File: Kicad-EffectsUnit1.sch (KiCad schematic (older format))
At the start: 114 parts, among them J101 In7, J102 Doepfer connector, J103 Vin 7-12v, J104 In6, J105 In3, J106 Out10, J107 Out11, J108 Out9, J109 Out6, J110 Power Conn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

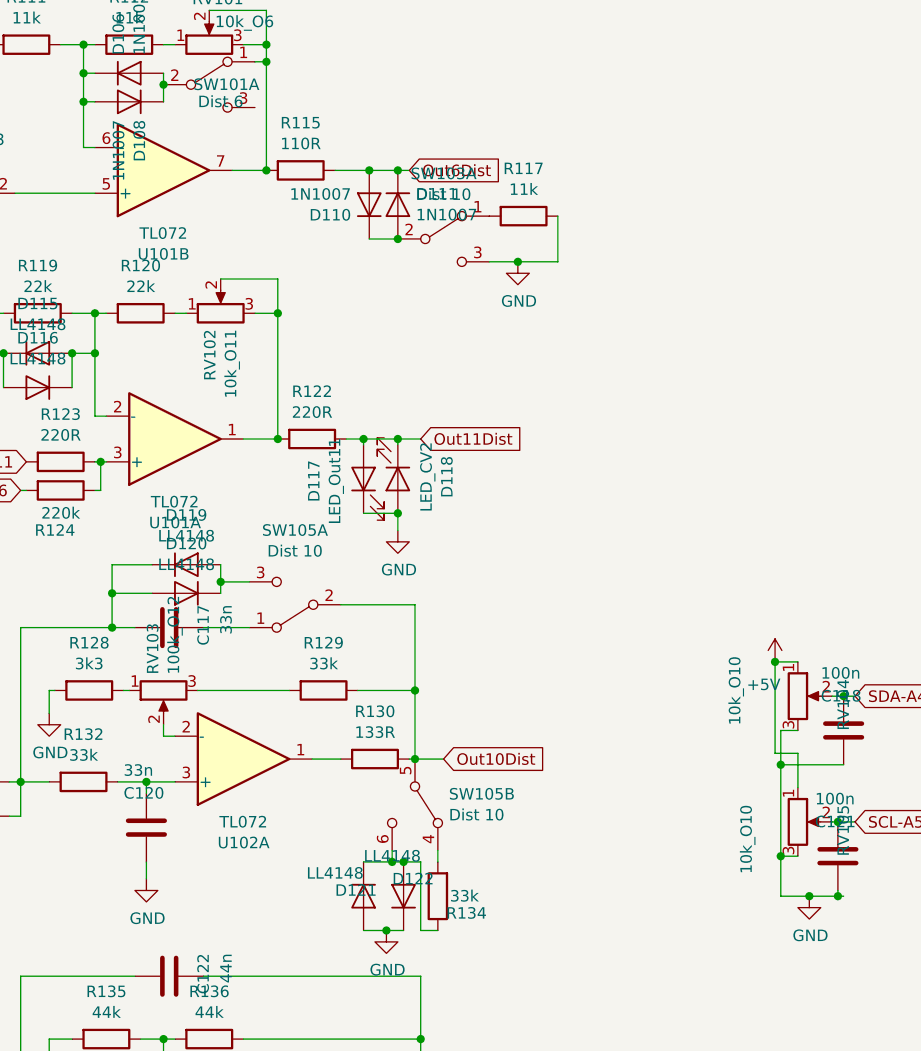
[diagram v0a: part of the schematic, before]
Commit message: sch pinout
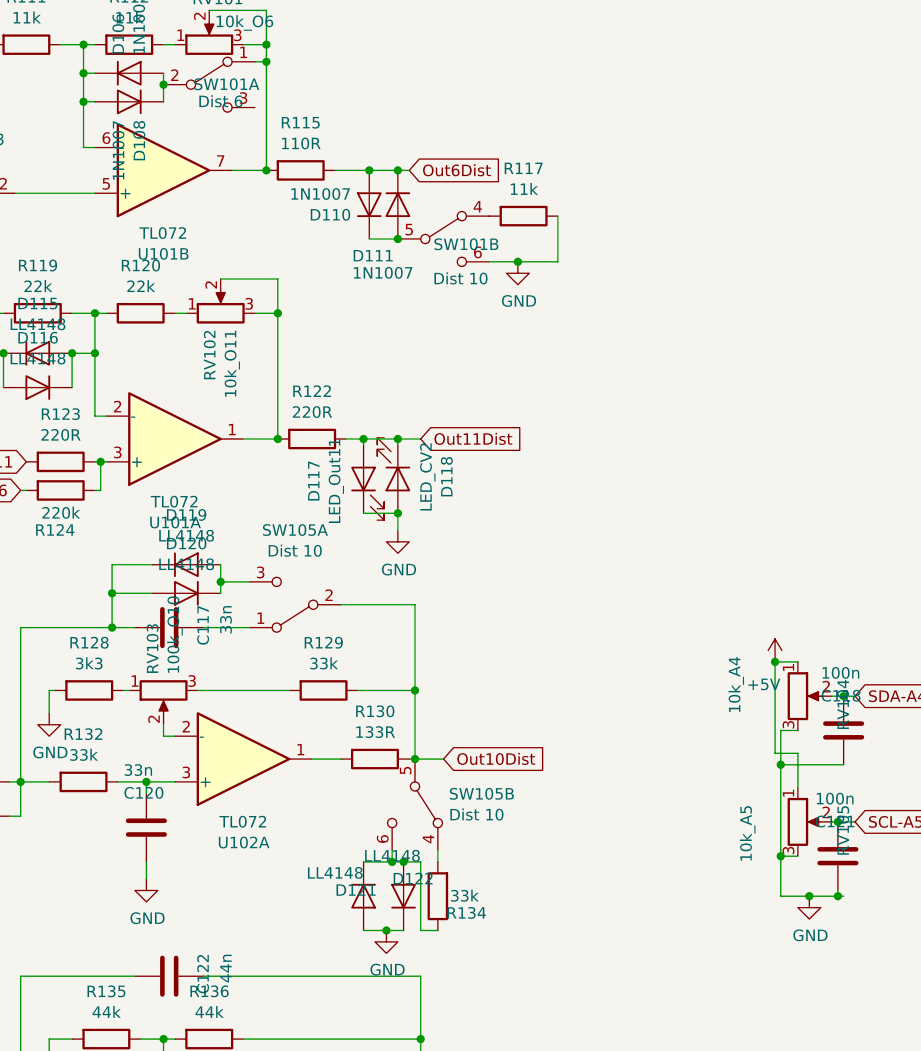
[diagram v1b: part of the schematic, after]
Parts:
- RV103: value 100k_O12 -> 100k_O10
- RV104: value 10k_O10 -> 10k_A4
- RV105: value 10k_O10 -> 10k_A5
- renumbered SW103 to SW101
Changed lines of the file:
@@
 U 1 1 5CCA754B
 P 6150 2925
-F 0 "D111" V 6104 3004 50  0000 L CNN
-F 1 "1N1007" V 6195 3004 50  0000 L CNN
+F 0 "D111" V 6375 2725 50  0000 L CNN
+F 1 "1N1007" V 6450 2725 50  0000 L CNN
 F 2 "Diode_SMD:D_SOD-123" H 6150 2925 50  0001 C CNN
 F 3 "~" H 6150 2925 50  0001 C CNN
@@
 $EndComp
 $Comp
-L Switch:SW_DPDT_x2 SW103
-U 1 1 5D077BCB
+L Switch:SW_DPDT_x2 SW101
+U 2 1 5D077BCB
 P 6350 3075
-F 0 "SW103" H 6350 3360 50  0000 C CNN
-F 1 "Dist 10" H 6350 3269 50  0000 C CNN
+F 0 "SW101" H 6450 3050 50  0000 C CNN
+F 1 "Dist 10" H 6425 2900 50  0000 C CNN
 F 2 "AJ-Dropbox-Kicad:SPDTx2" H 6350 3075 50  0001 C CNN
 F 3 "~" H 6350 3075 50  0001 C CNN
-	1    6350 3075
+	2    6350 3075
 	1    0    0    -1
 $EndComp
@@
 P 5125 5050
 F 0 "RV103" H 5055 5096 50  0000 R CNN
-F 1 "100k_O12" H 5055 5005 50  0000 R CNN
+F 1 "100k_O10" H 5055 5005 50  0000 R CNN
 F 2 "Potentiometer_THT:Potentiometer_China_RK09_Single_Vertical_AJ" H 5125 5050 50  0001 C CNN
 F 3 "~" H 5125 5050 50  0001 C CNN
@@
 P 7900 5075
 F 0 "RV104" V 8100 5150 50  0000 R CNN
-F 1 "10k_O10" V 7625 5250 50  0000 R CNN
+F 1 "10k_A4" V 7625 5250 50  0000 R CNN
 F 2 "Potentiometer_THT:Potentiometer_China_RK09_Single_Vertical_AJ" H 7900 5075 50  0001 C CNN
 F 3 "~" H 7900 5075 50  0001 C CNN
@@
 P 7900 5625
 F 0 "RV105" V 8100 5700 50  0000 R CNN
-F 1 "10k_O10" V 7675 5700 50  0000 R CNN
+F 1 "10k_A5" V 7675 5700 50  0000 R CNN
 F 2 "Potentiometer_THT:Potentiometer_China_RK09_Single_Vertical_AJ" H 7900 5625 50  0001 C CNN
 F 3 "~" H 7900 5625 50  0001 C CNN

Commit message: Removed components from PSU
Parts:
- removed C101: 100uF, Capacitor_THT:CP_Radial_D5.0mm_P2.50mm, symbol Device:CP
- removed C102, C103: 100n, Capacitor_SMD:C_0805_2012Metric_Pad1.15x1.40mm_HandSolder, symbol Device:C
- removed F102: Polyfuse, Fuse:Fuse_1206_3216Metric_Pad1.42x1.75mm_HandSolder, symbol Device:Polyfuse
- removed J103: Vin 7-12v, Connector_BarrelJack:BarrelJack_Horizontal, symbol Connector:Barrel_Jack_Switch
- removed J110: Power Conn, Connector_PinHeader_2.54mm:PinHeader_1x06_P2.54mm_Vertical, symbol Connector_Generic:Conn_01x06
- removed R102: 10M, Resistor_SMD:R_0805_2012Metric_Pad1.15x1.40mm_HandSolder, symbol Device:R
- SW101: value Dist 10 -> Dist 6
- SW102: value Crush A3 -> Crush A6
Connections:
- net labels removed: VCC
- wire segments 350 -> 330
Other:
- note removed: "POWER"
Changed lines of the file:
@@
 	950  2425 750  2425
-$Comp
-L Connector_Generic:Conn_01x06 J110
-U 1 1 5C21A17B
-P 2650 5375
-F 0 "J110" H 2750 5475 50  0000 L CNN
-F 1 "Power Conn" H 2450 5625 50  0000 L CNN
-F 2 "Connector_PinHeader_2.54mm:PinHeader_1x06_P2.54mm_Vertical" H 2650 5375 50  0001 C CNN
-F 3 "~" H 2650 5375 50  0001 C CNN
-	1    2650 5375
-	1    0    0    -1
-$EndComp
 $Comp
 L power:GND #PWR0116
@@
 $EndComp
 $Comp
-L Device:C C102
-U 1 1 5C22F1AA
-P 2050 1050
-F 0 "C102" H 2165 1096 50  0000 L CNN
-F 1 "100n" H 2165 1005 50  0000 L CNN
-F 2 "Capacitor_SMD:C_0805_2012Metric_Pad1.15x1.40mm_HandSolder" H 2088 900 50  0001 C CNN
-F 3 "~" H 2050 1050 50  0001 C CNN
-	1    2050 1050
-	1    0    0    -1
-$EndComp
-$Comp
-L Device:CP C101
-U 1 1 5C22F286
-P 1675 1050
-F 0 "C101" H 1793 1096 50  0000 L CNN
-F 1 "100uF" H 1793 1005 50  0000 L CNN
-F 2 "Capacitor_THT:CP_Radial_D5.0mm_P2.50mm" H 1713 900 50  0001 C CNN
-F 3 "~" H 1675 1050 50  0001 C CNN
-	1    1675 1050
-	1    0    0    -1
-$EndComp
-$Comp
-L Connector:Barrel_Jack_Switch J103
-U 1 1 5C22F3A0
-P 875 1050
-F 0 "J103" H 930 1375 50  0000 C CNN
-F 1 "Vin 7-12v" H 930 1284 50  0000 C CNN
-F 2 "Connector_BarrelJack:BarrelJack_Horizontal" H 925 1010 50  0001 C CNN
-F 3 "~" H 925 1010 50  0001 C CNN
-	1    875  1050
-	1    0    0    -1
-$EndComp
-Wire Wire Line
-	1500 950  1500 900
-Connection ~ 2050 900
-Wire Wire Line
-	1500 1150 1500 1200
-Wire Wire Line
-	1500 1200 1675 1200
-Connection ~ 2050 1200
-$Comp
 L Device:C C116
 U 1 1 5C289E13
@@
 $EndComp
 $Comp
-L power:VCC #PWR0102
-U 1 1 5C2979FB
-P 2050 900
-F 0 "#PWR0102" H 2050 750 50  0001 C CNN
-F 1 "VCC" H 2067 1073 50  0000 C CNN
-F 2 "" H 2050 900 50  0001 C CNN
-F 3 "" H 2050 900 50  0001 C CNN
-	1    2050 900
-	1    0    0    -1
-$EndComp
-$Comp
-L power:PWR_FLAG #FLG0101
-U 1 1 5C297A7B
-P 1675 900
-F 0 "#FLG0101" H 1675 975 50  0001 C CNN
-F 1 "PWR_FLAG" H 1675 1074 50  0000 C CNN
-F 2 "" H 1675 900 50  0001 C CNN
-F 3 "~" H 1675 900 50  0001 C CNN
-	1    1675 900
-	1    0    0    -1
-$EndComp
-$Comp
 L power:+5V #PWR0115
 U 1 1 5C29C771
@@
 F 3 "" H 1850 5350 50  0001 C CNN
 	1    1850 5350
-	1    0    0    -1
-$EndComp
-$Comp
-L power:GND #PWR0103
-U 1 1 5C293067
-P 2050 1200
-F 0 "#PWR0103" H 2050 950 50  0001 C CNN
-F 1 "GND" H 2055 1027 50  0000 C CNN
-F 2 "" H 2050 1200 50  0001 C CNN
-F 3 "" H 2050 1200 50  0001 C CNN
-	1    2050 1200
 	1    0    0    -1
 $EndComp
@@
 	1    3050 1050
 	-1   0    0    1
-$EndComp
-$Comp
-L power:VCC #PWR0114
-U 1 1 5C2A7BAB
-P 1550 5250
-F 0 "#PWR0114" H 1550 5100 50  0001 C CNN
-F 1 "VCC" H 1567 5423 50  0000 C CNN
-F 2 "" H 1550 5250 50  0001 C CNN
-F 3 "" H 1550 5250 50  0001 C CNN
-	1    1550 5250
-	1    0    0    -1
-$EndComp
-Wire Wire Line
-	1500 900  1675 900
-$Comp
-L Device:R R102
-U 1 1 5C2B290D
-P 2325 900
-F 0 "R102" V 2118 900 50  0000 C CNN
-F 1 "10M" V 2209 900 50  0000 C CNN
-F 2 "Resistor_SMD:R_0805_2012Metric_Pad1.15x1.40mm_HandSolder" V 2255 900 50  0001 C CNN
-F 3 "~" H 2325 900 50  0001 C CNN
-	1    2325 900
-	0    1    1    0
 $EndComp
 $Comp
@@
 	-1   0    0    1
 $EndComp
-Connection ~ 2750 1200
 Wire Wire Line
 	2750 1200 3050 1200
@@
 	1    0    0    -1
 $EndComp
-Wire Wire Line
-	3900 1300 4100 1300
 Connection ~ 4100 1300
 Wire Wire Line
@@
 Wire Wire Line
 	4500 1600 4700 1600
-Text Notes 650  650  0    79   ~ 16
-POWER
 Wire Notes Line
 	600  1400 600  500
@@
 Text GLabel 2400 2425 2    50   Input ~ 0
 LED4
-Text GLabel 2450 5675 0    50   Input ~ 0
--12V
-Text GLabel 2450 5475 0    50   Input ~ 0
-+12V
 $Comp
 L Device:C C112
@@
 	3050 1200 3275 1200
 Connection ~ 3050 1200
-Connection ~ 1675 900
-Wire Wire Line
-	1675 900  2050 900
-Connection ~ 1675 1200
-Wire Wire Line
-	1675 1200 2050 1200
-Wire Wire Line
-	2050 900  2175 900
-Wire Wire Line
-	2050 1200 2575 1200
-Wire Wire Line
-	2475 900  2575 900
-$Comp
-L Device:C C103
-U 1 1 5D1D00BC
-P 2575 1050
-F 0 "C103" H 2690 1096 50  0000 L CNN
-F 1 "100n" H 2690 1005 50  0000 L CNN
-F 2 "Capacitor_SMD:C_0805_2012Metric_Pad1.15x1.40mm_HandSolder" H 2613 900 50  0001 C CNN
-F 3 "~" H 2575 1050 50  0001 C CNN
-	1    2575 1050
-	-1   0    0    1
-$EndComp
-Connection ~ 2575 1200
-Wire Wire Line
-	2575 1200 2750 1200
-Connection ~ 2575 900
-Wire Wire Line
-	2575 900  3050 900
-Wire Wire Line
-	1500 1150 1175 1150
-$Comp
-L Device:Polyfuse F102
-U 1 1 5D47D22D
-P 1350 950
-F 0 "F102" V 1125 950 50  0000 C CNN
-F 1 "Polyfuse" V 1216 950 50  0000 C CNN
-F 2 "Fuse:Fuse_1206_3216Metric_Pad1.42x1.75mm_HandSolder" H 1400 750 50  0001 L CNN
-F 3 "~" H 1350 950 50  0001 C CNN
-	1    1350 950
-	0    1    1    0
-$EndComp
-Wire Wire Line
-	1175 950  1200 950
 $Comp
 L Device:D D101
@@
 P 4275 2875
 F 0 "SW102" H 4275 2550 50  0000 C CNN
-F 1 "Crush A3" H 4275 2641 50  0000 C CNN
+F 1 "Crush A6" H 4275 2641 50  0000 C CNN
 F 2 "AJ-Dropbox-Kicad:SP1MS1" H 4275 2875 50  0001 C CNN
 F 3 "~" H 4275 2875 50  0001 C CNN
@@
 	2125 5600 2125 5575
 Wire Wire Line
-	2125 5575 2450 5575
-Wire Wire Line
-	1550 5250 1550 5275
-Wire Wire Line
 	750  2725 750  2950
 Wire Wire Line
@@
 P 6350 3075
 F 0 "SW101" H 6450 3050 50  0000 C CNN
-F 1 "Dist 10" H 6425 2900 50  0000 C CNN
+F 1 "Dist 6" H 6425 2900 50  0000 C CNN
 F 2 "AJ-Dropbox-Kicad:SPDTx2" H 6350 3075 50  0001 C CNN
 F 3 "~" H 6350 3075 50  0001 C CNN
@@
 Text GLabel 1050 7125 0    50   Input ~ 0
 LED-Out11
+Text GLabel 4100 5600 0    50   Input ~ 0
+A3
 Text GLabel 4075 2775 0    50   Input ~ 0
-A3
+A6
 Text GLabel 4500 4175 0    50   Input ~ 0
-A6
-Text GLabel 4100 5600 0    50   Input ~ 0
 A7
 $Comp
@@
 $EndComp
 Wire Wire Line
-	2125 5375 2450 5375
-Connection ~ 2125 5575
-Wire Wire Line
 	2125 5375 1850 5375
-Connection ~ 2125 5375
 Connection ~ 1850 5375
 Wire Wire Line
 	1850 5375 1850 5425
-Wire Wire Line
-	2450 5275 1550 5275
-Connection ~ 1550 5275
-Wire Wire Line
-	1550 5275 1550 5425
-Wire Wire Line
-	2450 5175 1750 5175
-Wire Wire Line
-	1750 5175 1750 5425
 $Sheet
 S 8675 4700 2400 1725
@@
 F1 "KicadJE-EU1-PT2399_sub.sch" 50
 $EndSheet
-Wire Wire Line
-	1175 1050 1500 1050
-Wire Wire Line
-	1500 1050 1500 1150
-Connection ~ 1500 1150
 Text GLabel 8150 5625 2    50   Input ~ 0
 SCL-A5
@@
 Wire Wire Line
 	7825 5375 7825 5775
+Wire Wire Line
+	3275 1300 3275 1200
+Wire Wire Line
+	3275 1300 3900 1300
+Connection ~ 3900 1300
+Wire Wire Line
+	3900 1300 4100 1300
+Connection ~ 3275 1200
 $EndSCHEMATC

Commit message: misc
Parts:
- D117: value LED_Out11 -> LED_11dist
- D118: value LED_CV2 -> LED_11dist
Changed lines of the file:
@@
 P 6150 4125
 F 0 "D118" H 6141 4341 50  0000 C CNN
-F 1 "LED_CV2" H 6141 4250 50  0000 C CNN
+F 1 "LED_11dist" H 6141 4250 50  0000 C CNN
 F 2 "LED_THT:LED_D3.0mm" H 6150 4125 50  0001 C CNN
 F 3 "~" H 6150 4125 50  0001 C CNN
@@
 P 6000 4125
 F 0 "D117" H 5991 4341 50  0000 C CNN
-F 1 "LED_Out11" H 5991 4250 50  0000 C CNN
+F 1 "LED_11dist" H 5991 4250 50  0000 C CNN
 F 2 "LED_SMD:LED_0805_2012Metric_Pad1.15x1.40mm_HandSolder" H 6000 4125 50  0001 C CNN
 F 3 "~" H 6000 4125 50  0001 C CNN

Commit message: PREPARE for major restruct
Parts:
- removed C109, C113: 100n, Capacitor_SMD:C_0805_2012Metric_Pad1.15x1.40mm_HandSolder, symbol Device:C
- D110, D111: footprint Diode_SMD:D_SOD-123 -> Diode_SMD:D_0805_2012Metric_Pad1.15x1.40mm_HandSolder
- D118: footprint LED_THT:LED_D3.0mm -> Diode_SMD:D_0805_2012Metric_Pad1.15x1.40mm_HandSolder
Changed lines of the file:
@@
 Connection ~ 4700 1000
-$Comp
-L Device:C C109
-U 1 1 5D4AC35B
-P 4875 1150
-F 0 "C109" H 4925 1050 50  0000 L CNN
-F 1 "100n" H 4825 950 50  0000 L CNN
-F 2 "Capacitor_SMD:C_0805_2012Metric_Pad1.15x1.40mm_HandSolder" H 4913 1000 50  0001 C CNN
-F 3 "~" H 4875 1150 50  0001 C CNN
-	1    4875 1150
-	-1   0    0    1
-$EndComp
-Connection ~ 4875 1300
-Wire Wire Line
-	4875 1300 5000 1300
-Connection ~ 4875 1000
-Wire Wire Line
-	4875 1000 4950 1000
-$Comp
-L Device:C C113
-U 1 1 5D4AC43F
-P 4875 1450
-F 0 "C113" H 4775 1600 50  0000 L CNN
-F 1 "100n" H 4775 1700 50  0000 L CNN
-F 2 "Capacitor_SMD:C_0805_2012Metric_Pad1.15x1.40mm_HandSolder" H 4913 1300 50  0001 C CNN
-F 3 "~" H 4875 1450 50  0001 C CNN
-	1    4875 1450
-	-1   0    0    1
-$EndComp
-Connection ~ 4875 1600
-Wire Wire Line
-	4875 1600 5150 1600
-Wire Wire Line
-	4700 1000 4875 1000
-Wire Wire Line
-	4700 1300 4875 1300
-Wire Wire Line
-	4700 1600 4875 1600
 $Comp
 L Amplifier_Operational:TL072 U102
@@
 F 0 "D111" V 6375 2725 50  0000 L CNN
 F 1 "1N1007" V 6450 2725 50  0000 L CNN
-F 2 "Diode_SMD:D_SOD-123" H 6150 2925 50  0001 C CNN
+F 2 "Diode_SMD:D_0805_2012Metric_Pad1.15x1.40mm_HandSolder" H 6150 2925 50  0001 C CNN
 F 3 "~" H 6150 2925 50  0001 C CNN
 	1    6150 2925
@@
 F 0 "D110" V 5979 3004 50  0000 L CNN
 F 1 "1N1007" V 6070 3004 50  0000 L CNN
-F 2 "Diode_SMD:D_SOD-123" H 6025 2925 50  0001 C CNN
+F 2 "Diode_SMD:D_0805_2012Metric_Pad1.15x1.40mm_HandSolder" H 6025 2925 50  0001 C CNN
 F 3 "~" H 6025 2925 50  0001 C CNN
 	1    6025 2925
@@
 F 0 "D118" H 6141 4341 50  0000 C CNN
 F 1 "LED_11dist" H 6141 4250 50  0000 C CNN
-F 2 "LED_THT:LED_D3.0mm" H 6150 4125 50  0001 C CNN
+F 2 "Diode_SMD:D_0805_2012Metric_Pad1.15x1.40mm_HandSolder" H 6150 4125 50  0001 C CNN
 F 3 "~" H 6150 4125 50  0001 C CNN
 	1    6150 4125
@@
 	3900 1300 4100 1300
 Connection ~ 3275 1200
+Wire Wire Line
+	4700 1000 4950 1000
+Wire Wire Line
+	4700 1600 5150 1600
+Wire Wire Line
+	4700 1300 5000 1300
 $EndSCHEMATC

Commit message: Remove extra components from PT2399 and add EU3 diagram
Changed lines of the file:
@@
 $Descr A4 11693 8268
 encoding utf-8
-Sheet 1 2
+Sheet 1 3
 Title "Effects Unit 1"
 Date "2019-02-05"
@@
 Wire Wire Line
 	4700 1300 5000 1300
+$Sheet
+S 6875 750  2525 1800
+U 5C781441
+F0 "EU3" 50
+F1 "EU3.sch" 50
+$EndSheet
 $EndSCHEMATC
